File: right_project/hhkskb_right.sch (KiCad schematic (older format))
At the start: 76 parts, among them J1 4pin_Jack, SW11 SW_PUSH, SW12 SW_PUSH, SW13 SW_PUSH, SW14 SW_PUSH, SW15 SW_PUSH, SW16 SW_PUSH, SW17 SW_PUSH, SW21 SW_PUSH, SW22 SW_PUSH, SW23 SW_PUSH, SW24 SW_PUSH, SW25 SW_PUSH, SW26 SW_PUSH, SW27 SW_PUSH, SW28 SW_PUSH, SW31 SW_PUSH, SW32 SW_PUSH, SW33 SW_PUSH, SW34 SW_PUSH, SW35 SW_PUSH, SW36 SW_PUSH, SW37 SW_PUSH, SW41 SW_PUSH, SW42 SW_PUSH, SW43 SW_PUSH, SW44 SW_PUSH, SW45 SW_PUSH, SW46 SW_PUSH, SW47 SW_PUSH, SW48 SW_PUSH, SW51 SW_PUSH, SW52 SW_PUSH, SW53 SW_PUSH, SW54 SW_PUSH, SW55 SW_PUSH, SW56 SW_PUSH, SW57 SW_PUSH, U1 ARDUINO_MICRO_SHIELD

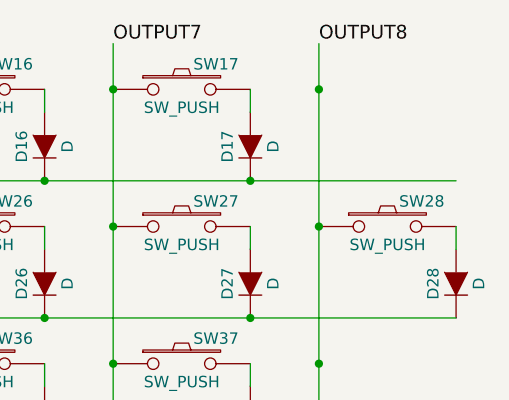
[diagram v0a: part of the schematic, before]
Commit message: キーレイアウト変更 *  一行目7キーを2つに分離 ** バックスラッシュとにょろで使う。 ** 二行目8キーはDeleteに変更 M2ねじのホール定義を変更 * 穴を2.5に変更 * ランドをねじ頭分3.5用意 ねじ穴を大量に用意
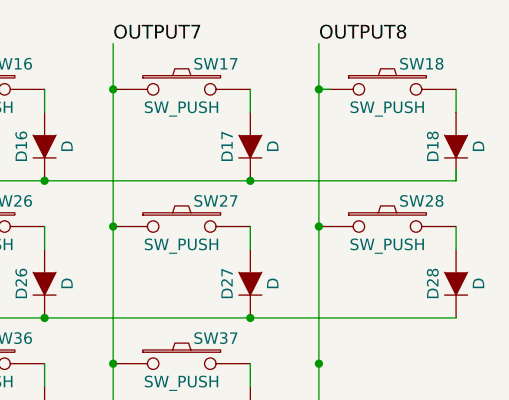
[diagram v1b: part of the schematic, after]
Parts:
- added D18: D, Discret:DO-41, symbol D
- added SW18: SW_PUSH, MyFootprint:CHERRY_PLATE_100H, symbol SW_PUSH
- SW17: footprint MyFootprint:CHERRY_PLATE_200H -> MyFootprint:CHERRY_PLATE_100H
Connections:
- wire segments 61 -> 64
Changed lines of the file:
@@
 F 0 "SW17" H 9850 1160 50  0000 C CNN
 F 1 "SW_PUSH" H 9700 970 50  0000 C CNN
-F 2 "MyFootprint:CHERRY_PLATE_200H" H 9700 1050 50  0001 C CNN
+F 2 "MyFootprint:CHERRY_PLATE_100H" H 9700 1050 50  0001 C CNN
 F 3 "" H 9700 1050 50  0000 C CNN
 	1    9700 1050
@@
 $EndComp
 $Comp
-L GND #PWR?
+L GND #PWR09
 U 1 1 5889649A
 P 2950 5300
-F 0 "#PWR?" H 2950 5050 50  0001 C CNN
+F 0 "#PWR09" H 2950 5050 50  0001 C CNN
 F 1 "GND" H 2950 5150 50  0000 C CNN
 F 2 "" H 2950 5300 50  0000 C CNN
@@
 Wire Wire Line
 	2950 5250 2950 5300
+$Comp
+L SW_PUSH SW18
+U 1 1 5895E000
+P 10600 1050
+F 0 "SW18" H 10750 1160 50  0000 C CNN
+F 1 "SW_PUSH" H 10600 970 50  0000 C CNN
+F 2 "MyFootprint:CHERRY_PLATE_100H" H 10600 1050 50  0001 C CNN
+F 3 "" H 10600 1050 50  0000 C CNN
+	1    10600 1050
+	1    0    0    -1
+$EndComp
+$Comp
+L D D18
+U 1 1 5895E121
+P 10900 1300
+F 0 "D18" H 10900 1400 50  0000 C CNN
+F 1 "D" H 10900 1200 50  0000 C CNN
+F 2 "Discret:DO-41" H 10900 1300 50  0001 C CNN
+F 3 "" H 10900 1300 50  0000 C CNN
+	1    10900 1300
+	0    -1   -1   0
+$EndComp
+Wire Wire Line
+	10900 1450 10900 1400
+Wire Wire Line
+	10300 1050 10350 1050
+Wire Wire Line
+	10900 1150 10900 1050
 $EndSCHEMATC
